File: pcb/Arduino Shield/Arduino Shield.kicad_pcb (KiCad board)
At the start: 2 copper layers, 101.6 x 53.3 mm, 45 parts, among them J1 Power, J10 CH_02, J11 CH_03, J12 CH_04, J13 CH_05, J14 Main, J15 DRV_03, J16 DRV_02, J17 DRV_01, J18 EXT VCC, J19 DRV_03_PWR, J2 PWM, J20 SD_SPI, J21 DRV_02_PWR, J22 DRV_01_PWR, J3 Analog, J4 PWM, J5 Analog, J6 Communication, J7 Digital, J8 SCR_SPI, J9 CH_01

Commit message: Update pcb, start channel
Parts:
- added J23: Power SW, Connector_PinSocket_2.00mm:PinSocket_1x02_P2.00mm_Vertical, F.Cu at (162.0, 84.5)
- F1: footprint Fuse:Fuseholder_Cylinder-5x20mm_Stelvio-Kontek_PTF78_Horizontal_Open -> Fuse:Fuseholder_Clip-5x20mm_Eaton_1A5601-01_Inline_P20.80x6.76mm_D1.70mm_Horizontal
- J14: value Main -> Main Controller
- moved J18 25.7 mm to (162.0, 58.5), turned to 180 degrees
- moved C6 6.00 mm to (140.5, 65.5)
- moved C7 6.00 mm to (147.0, 65.5)
- moved C8 6.00 mm to (152.5, 65.5)
- moved J15 6.00 mm to (152.5, 77.0)
- moved J16 6.00 mm to (147.0, 77.0)
- moved J17 6.00 mm to (140.5, 77.0)
- moved J19 6.00 mm to (152.5, 70.0)
- moved J21 6.00 mm to (147.0, 70.0)
- moved J22 6.00 mm to (140.5, 70.0)
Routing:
- net CH2_SCR_CS: track 96.9 -> 70.8 mm, vias 3 -> 0
- net Net-(J23-Pin_2): track 0.00 -> 16.8 mm
- net CH5_SCR_DC: track 74.9 -> 91.5 mm, vias 0 -> 2
- net CH5_ENC_DT: track 94.0 -> 78.0 mm, vias 2 -> 0
- net E_VCC: track 191.4 -> 206.8 mm, vias 1 -> 2
- net CH1_MOTOR_B: track 38.6 -> 53.1 mm, vias 1 -> 2
- net Net-(J18-Pin_1): track 46.3 -> 32.5 mm
- net +5V: track 108.9 -> 96.5 mm, vias 2 -> 1
- net CH5_ENC_SW: track 89.8 -> 77.5 mm, vias 4 -> 0
- net CH4_MOTOR_B: track 31.8 -> 43.6 mm, vias 0 -> 1
- net CH_MAIN_SCR_CS: track 60.1 -> 49.0 mm, vias 2 -> 1
- net CH2_FADER_OUT: track 64.6 -> 75.7 mm
- net CH1_MOTOR_A: track 37.3 -> 46.0 mm, vias 2 -> 1
- net CH2_MOTOR_B: track 38.7 -> 47.0 mm
- net CH3_MOTOR_B: track 24.3 -> 32.5 mm
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
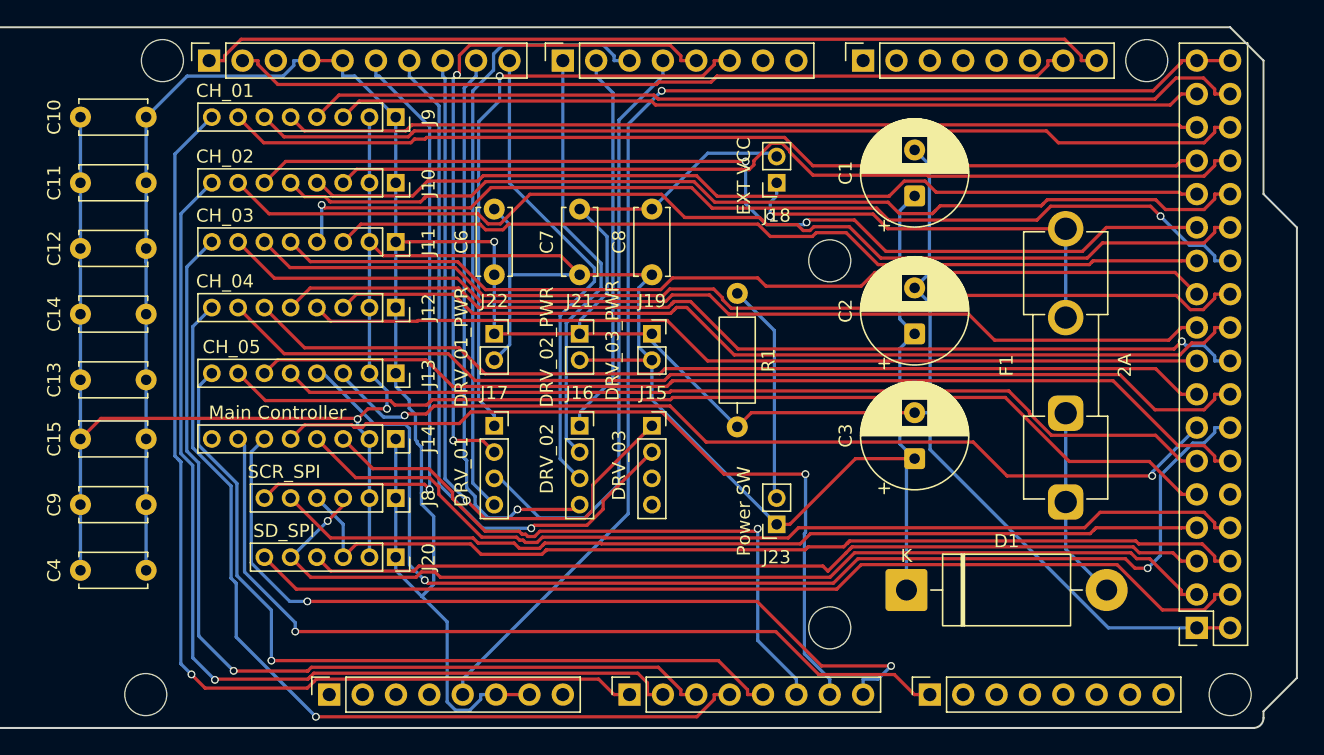
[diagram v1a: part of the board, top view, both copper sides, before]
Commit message: Update main PCB to use 9pin connectors for channels (They need unique RST)
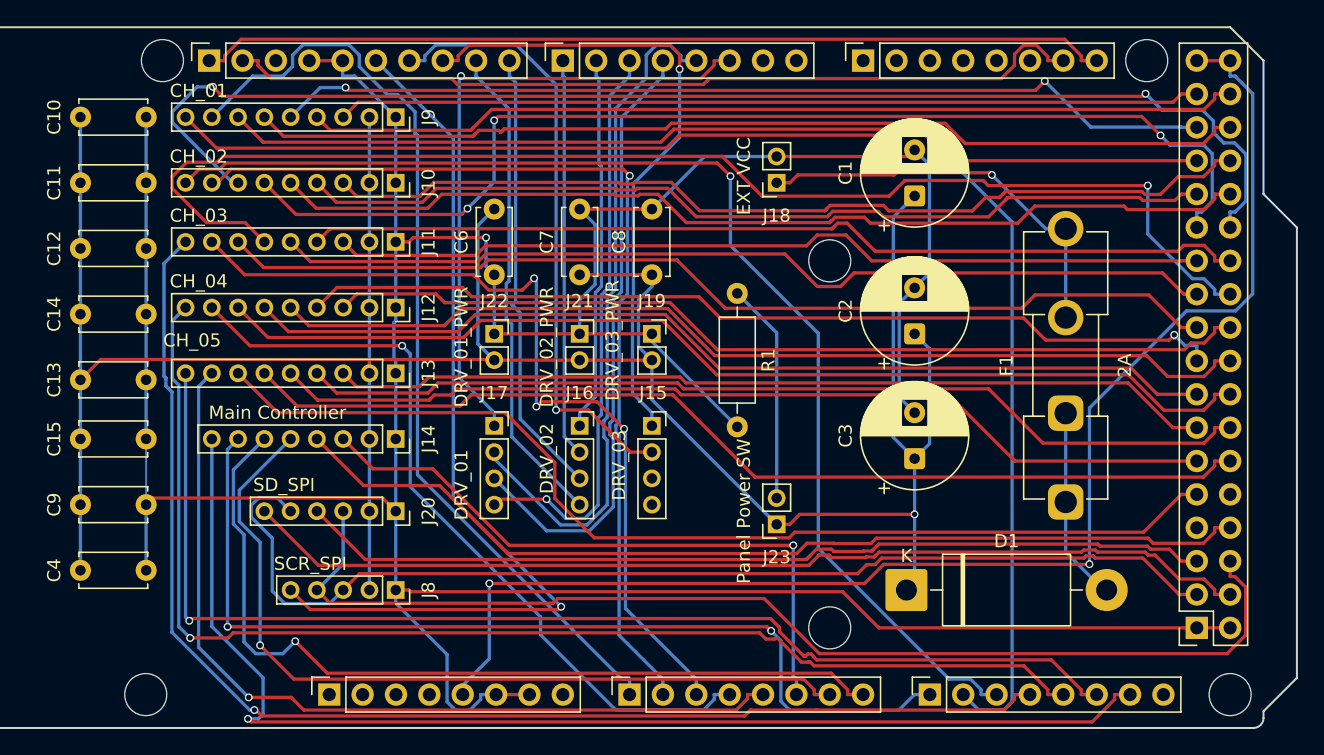
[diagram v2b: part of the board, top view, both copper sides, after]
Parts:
- J10, J11, J12, J13, J9: footprint Connector_PinSocket_2.00mm:PinSocket_1x08_P2.00mm_Vertical -> Connector_PinSocket_2.00mm:PinSocket_1x09_P2.00mm_Vertical
- J23: value Power SW -> Panel Power SW
- J8: footprint Connector_PinSocket_2.00mm:PinSocket_1x06_P2.00mm_Vertical -> Connector_PinSocket_2.00mm:PinSocket_1x05_P2.00mm_Vertical
- moved J8 7.00 mm to (133.0, 89.5)
- moved J20 3.50 mm to (133.0, 83.5)
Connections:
- J14 pad 8: unconnected-(J14-Pin_8-Pad8) -> MAIN_SCR_RST
- J5 pad 2: /A9 -> CH1_SCR_RST
- J5 pad 3: /A10 -> CH2_SCR_RST
- J5 pad 4: /A11 -> CH3_SCR_RST
- J5 pad 5: /A12 -> CH4_SCR_RST
- J5 pad 6: /A13 -> CH5_SCR_RST
- J5 pad 7: /A14 -> MAIN_SCR_RST
- J8 pad 5: SHARED_RST -> SCR_BL_PWM
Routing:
- net CH1_SCR_RST: track 0.00 -> 108.0 mm, vias 0 -> 1
- net CH3_SCR_RST: track 0.00 -> 100.3 mm, vias 0 -> 1
- net CH4_SCR_RST: track 0.00 -> 95.0 mm, vias 0 -> 1
- net MAIN_SCR_RST: track 0.00 -> 92.2 mm, vias 0 -> 1
- net CH2_SCR_RST: track 0.00 -> 92.0 mm, vias 0 -> 1
- net CH5_SCR_RST: track 0.00 -> 91.1 mm, vias 0 -> 1
- net SHARED_RST: track 71.7 -> 0.00 mm
- net CH3_ENC_DT: track 77.6 -> 98.7 mm, vias 0 -> 1
- net SCR_BL_PWM: track 47.7 -> 68.7 mm
- net CH5_SCR_DC: track 91.5 -> 73.1 mm, vias 2 -> 0
- net CH2_ENC_SW: track 81.2 -> 99.3 mm, vias 0 -> 2
- net GND: track 258.1 -> 272.5 mm
- net SPI_MOSI: track 75.5 -> 86.8 mm
- net CH2_ENC_DT: track 77.4 -> 86.5 mm, vias 2 -> 3
- net CH4_FADER_OUT: track 68.2 -> 59.5 mm
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
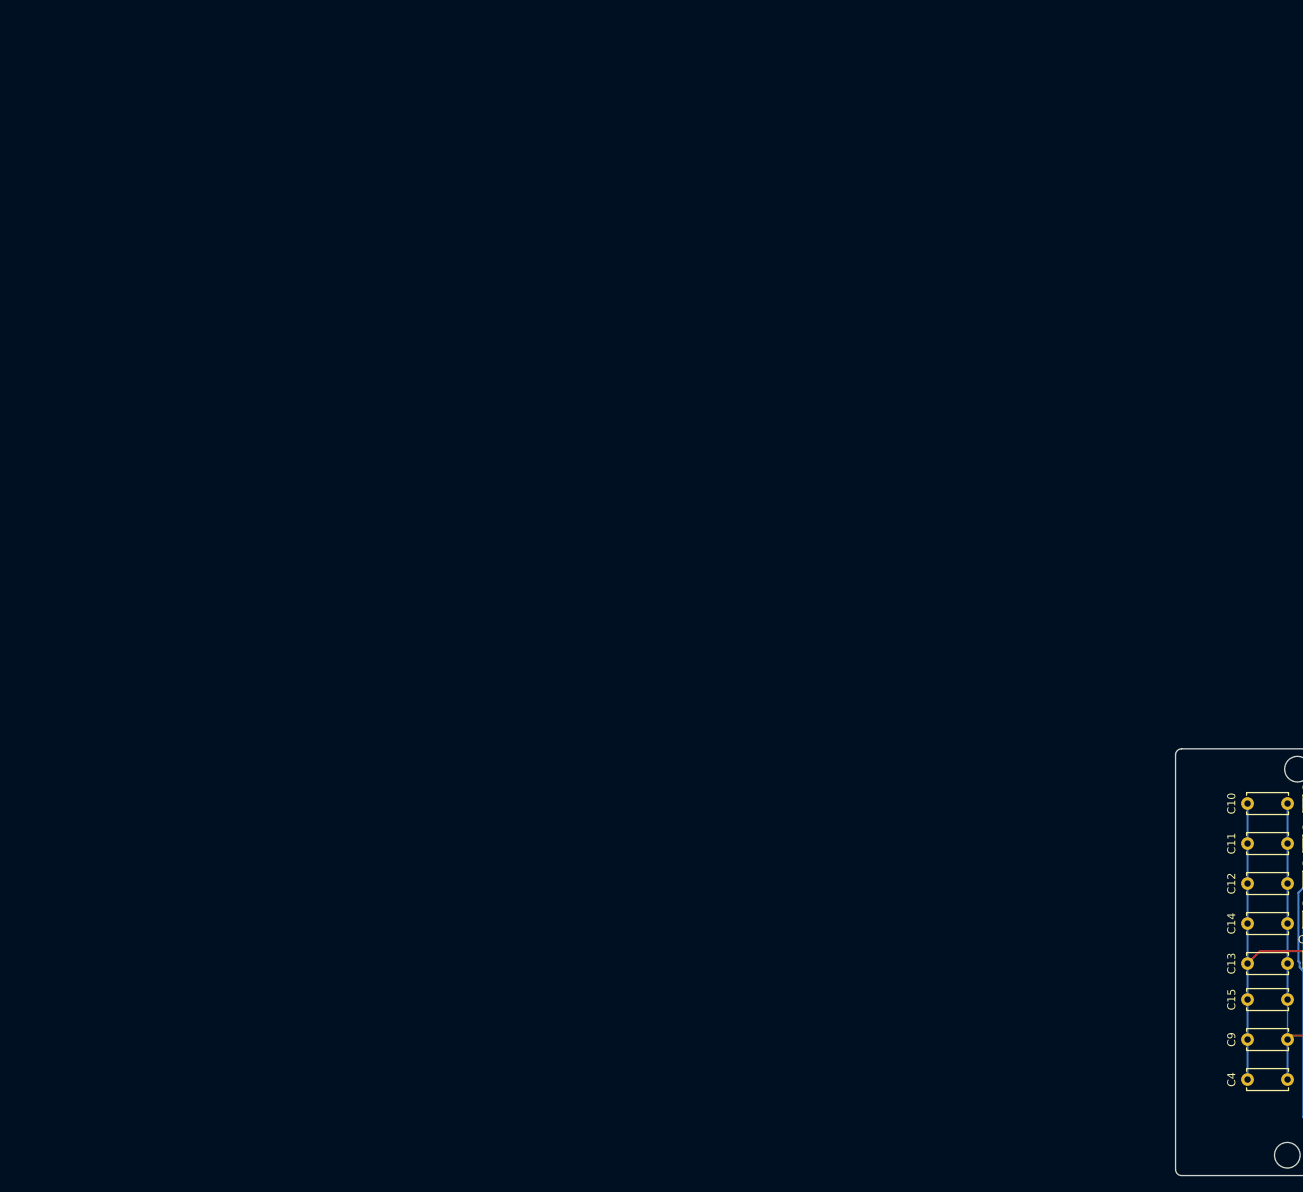
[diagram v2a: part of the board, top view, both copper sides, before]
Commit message: Update main pcb silkscreen.
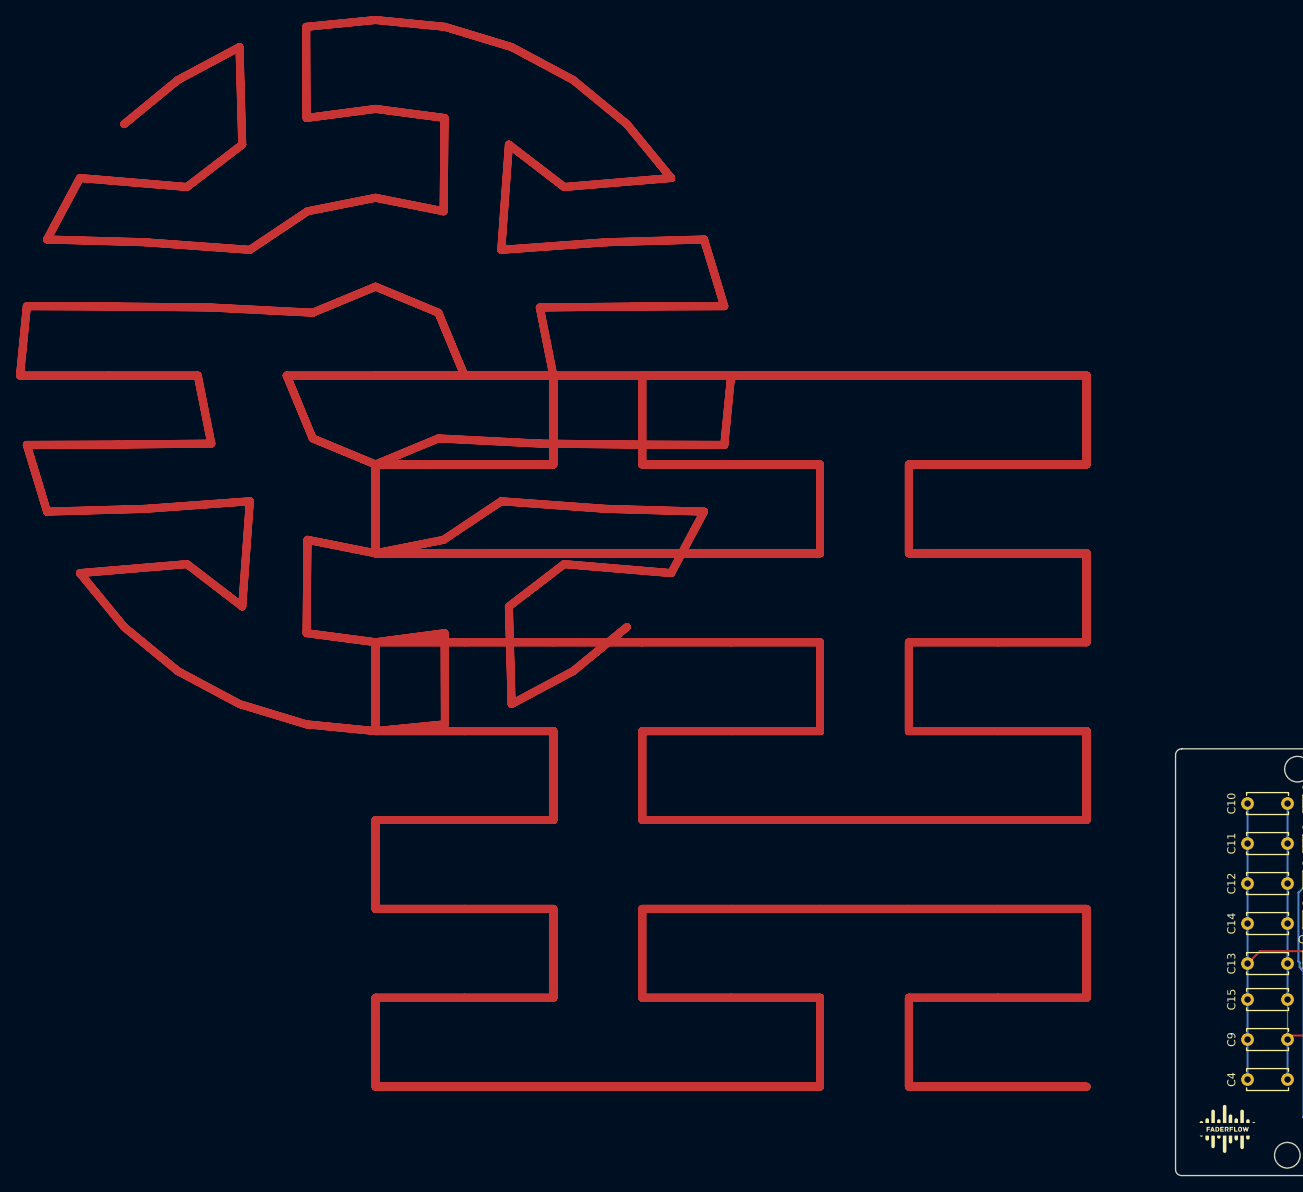
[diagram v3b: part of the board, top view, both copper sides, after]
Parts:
- added G***: LOGO, LOGO, F.Cu at (106.5, 94.5)
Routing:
- net (no net): track 0.00 -> 4302.9 mm
